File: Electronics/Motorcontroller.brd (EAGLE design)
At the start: 101.3 x 50.8 mm, 39 parts, among them Q1 IRFZ48V, Q2 IRF4905V, Q3 IRFZ48V, Q4 IRF4905V, Q5 IRFZ48V, Q6 IRF4905V, Q7 IRFZ48V, Q8 IRF4905V, T1 BC547, T2 BC547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

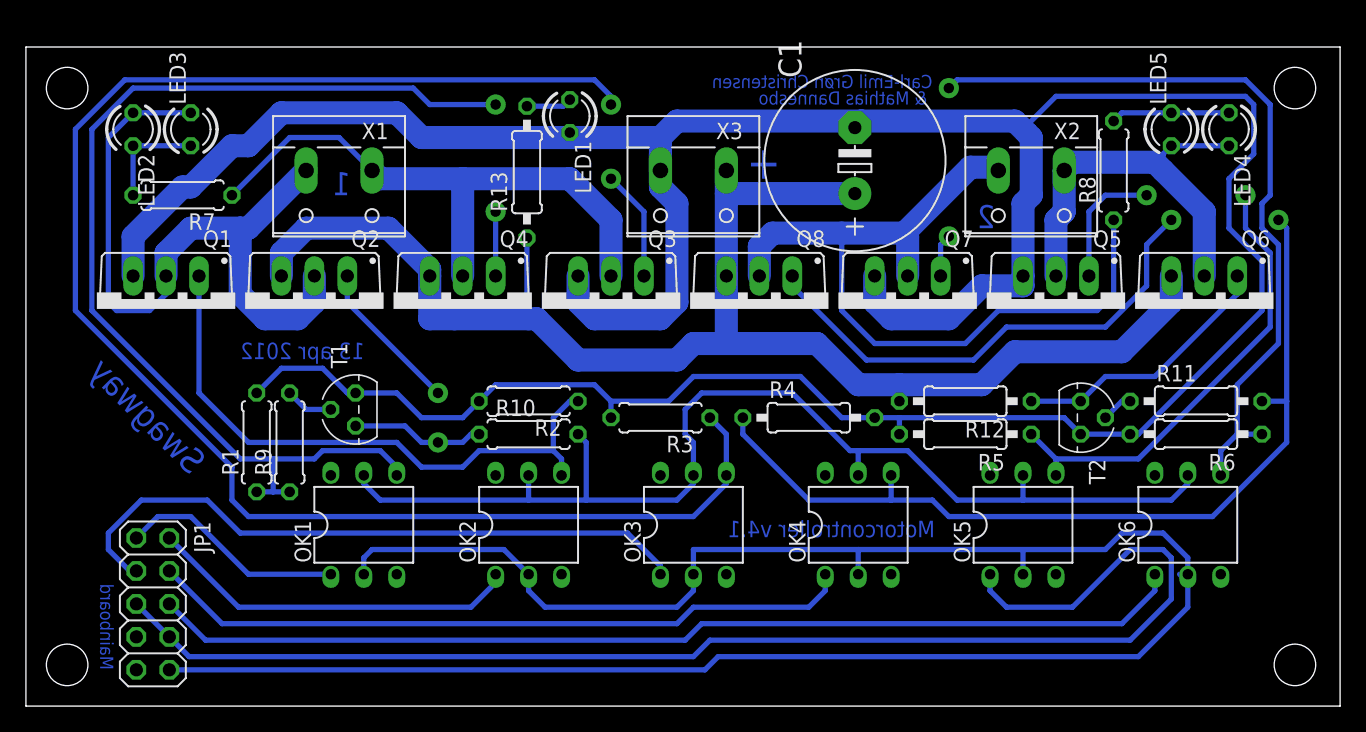
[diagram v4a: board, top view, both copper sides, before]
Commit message: Fixed airwire in motorboard. Updated .pdf and rapport
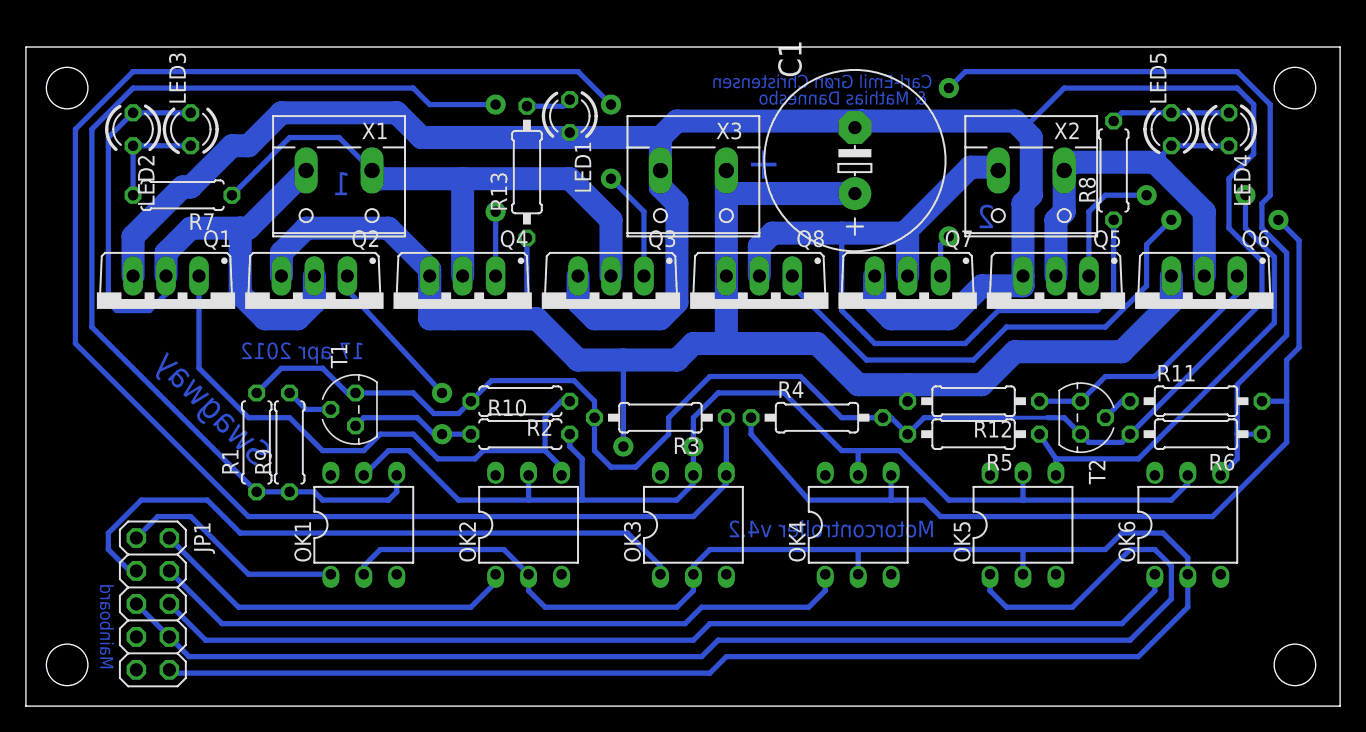
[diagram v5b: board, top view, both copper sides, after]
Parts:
- R3: device rcl:0207/7 -> rcl:0207/10
- moved R12 0.64 mm to (72.4, 54.6)
- moved R4 0.64 mm to (60.3, 53.3)
- moved R5 0.64 mm to (72.4, 52.1)
- moved R10 0.63 mm to (37.5, 52.1)
- moved R2 0.63 mm to (37.5, 54.6)
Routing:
- net +24V: track 203.7 -> 211.1 mm, vias 0 -> 1
- net GND2: track 258.8 -> 265.2 mm
- net N$12: track 86.6 -> 83.7 mm
- net GND: track 161.0 -> 159.8 mm
- net N$22: track 62.2 -> 63.3 mm
- net N$9: track 46.4 -> 45.4 mm
- net N$15: track 22.2 -> 21.5 mm
- net N$19: track 20.7 -> 20.1 mm
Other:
- board text added: "17 apr 2012"
- board text added: "Motorcontroller v4.2"
- board text removed: "13 apr 2012"
- board text removed: "Motorcontroller v4.1"

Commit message: Moved resistors to Motorboard. Closes #37
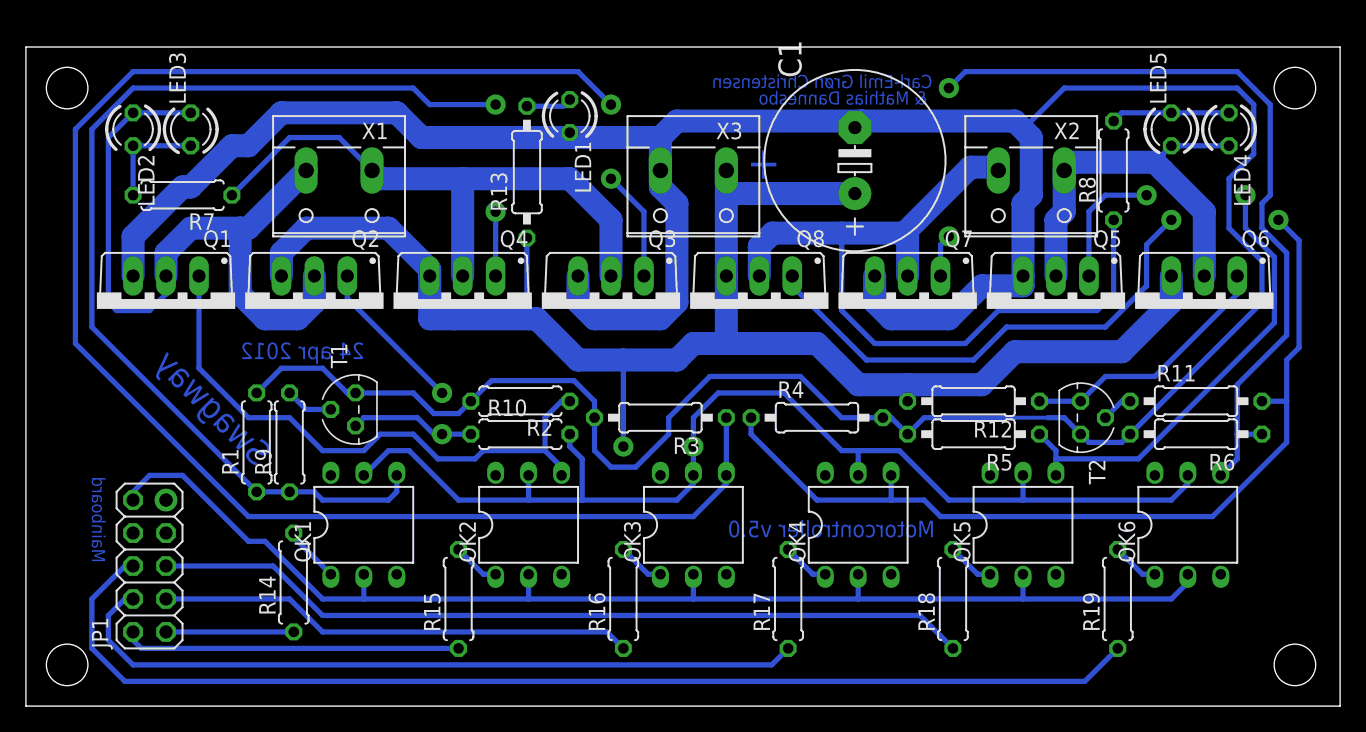
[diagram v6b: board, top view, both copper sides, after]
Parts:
- added R14, R15, R16, R17, R18, R19: 330, rcl:0207/7
- moved JP1 2.93 mm to (8.89, 41.9), turned to 90 degrees
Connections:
- new net N$29: OK1.1, R14.2
- new net N$30: OK2.1, R15.2
- new net N$31: OK3.1, R16.2
- new net N$32: OK4.1, R17.2
- new net N$36: OK5.1, R18.2
- new net N$37: OK6.1, R19.2
- net N$10: now also R18.1; no longer OK5.1
- net N$11: now also R19.1; no longer OK6.1
- net N$3: now also R14.1; no longer OK1.1
- net N$5: now also R15.1; no longer OK2.1
- net N$7: now also R16.1; no longer OK3.1
- net N$8: now also R17.1; no longer OK4.1
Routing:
- net GND: track 159.8 -> 97.1 mm
- net N$10: track 104.0 -> 63.3 mm
- net N$7: track 50.4 -> 36.8 mm
- net N$11: track 80.0 -> 89.2 mm
- net N$3: track 17.5 -> 9.84 mm
- net N$29: track 0.00 -> 4.36 mm
- net N$37: track 0.00 -> 3.65 mm
- net N$36: track 0.00 -> 3.65 mm
- net N$32: track 0.00 -> 3.65 mm
- net N$30: track 0.00 -> 3.65 mm
- net N$31: track 0.00 -> 3.65 mm
- net N$8: track 54.6 -> 58.0 mm
- net N$5: track 28.8 -> 26.0 mm
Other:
- board text added: "24 apr 2012"
- board text added: "Motorcontroller v5.0"
- board text removed: "1"
- board text removed: "17 apr 2012"
- board text removed: "2"
- board text removed: "Motorcontroller v4.2"
